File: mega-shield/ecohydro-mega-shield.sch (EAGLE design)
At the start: 99 parts, among them IC1 MCP1700-330, IC2 DS1306E, IC3 74HC125D, IC4 AP3211KTR, Q1 IRLM5103, Q10 PBSS4021NT,215, Q11 PBSS4021NT,215, Q12 PBSS4021NT,215, Q13 PBSS4021NT,215, Q14 PBSS4021NT,215, Q15 PBSS4021NT,215, Q16 PBSS4021NT,215, Q17 IRLM5103, Q18 IRLM5103, Q19 IRLM5103, Q2 IRLM5103, Q20 PBSS4021NT,215, Q21 PBSS4021NT,215, Q22 PBSS4021NT,215, Q3 IRLM5103, Q4 IRLM5103, Q5 IRLM5103, Q6 IRLM5103, Q7 IRLM5103, Q8 IRLM5103, Q9 PBSS4021NT,215, U1 ARDUINO-MEGA

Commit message: Rev 1.1 with some fixes, not sent for production yet
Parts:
- removed A7: MKDS1/3-3,81, con-phoenix-381:MKDS1/3-3,81
- added A15: MKDS1/3-3,81, con-phoenix-381:MKDS1/3-3,81
- BATT1: DIGIKEY (none) -> BK-883CT-ND
- C5: DIGIKEY (none) -> 490-1664-1-ND
- C6: DIGIKEY (none) -> 1276-2891-1-ND
- C7: DIGIKEY (none) -> 709-1231-1-ND
- D1: DIGIKEY (none) -> S1GFSCT-ND
- FS1, FS2: ATTRIBUTE 576-65800001109 -> (none); MOUSER (none) -> 576-65800001109
- IC1: DIGIKEY (none) -> AP1117IE33G-13DITR-ND
- IC2: DIGIKEY (none) -> DS1306EN+T&RCT-ND
- IC3: DIGIKEY (none) -> 568-1392-2-ND
- IC4: DIGIKEY (none) -> AP3211KTR-G1DICT-ND
- L1: DIGIKEY (none) -> 732-5536-1-ND
- Q10, Q11, Q12, Q13, Q14, Q15, Q16, Q20, Q21, Q22, Q9: DIGIKEY (none) -> PBSS4021NT,215
- R11, R12, R13, R14, R15, R16, R17, R18: DIGIKEY (none) -> 541-330ACT-ND
- R19: value 470R -> 1k; device passives:R-EU_R0603-N -> passives:R-EU_R0805
- R23: DIGIKEY (none) -> 541-49.9KCCT-ND
- R24: DIGIKEY (none) -> 541-9.53KCCT-ND
- Y1: DIGIKEY (none) -> 535-12051-1-ND
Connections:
- removed net N$5 (its old number): A7-2.1, U1.A7
- new net N$76: U1.3
- new net N$77: U1.2
- new net N$88: A15-2.1, U1.A15
- net GND: now also A15-3.1; no longer A7-3.1
- net N$10: now also A14-1.1; no longer A13-1.1
- net N$11: now also A13-1.1; no longer A12-1.1
- net N$12: now also A12-1.1; no longer A11-1.1
- net N$13: now also A11-1.1; no longer A10-1.1
- net N$14: now also U1.20(SDA); no longer U1.5
- net N$4: now also A8-1.1; no longer A7-1.1
- net N$6: now also A9-1.1; no longer A8-1.1
- net N$73: no longer U1.3
- net N$75: no longer U1.4
- net N$8: now also A10-1.1; no longer A9-1.1
- net N$9: now also A15-1.1; no longer A14-1.1
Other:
- moved on the sheet: A10-1, A10-2, A10-3, A11-1, A11-2, A11-3, A12-1, A12-2, A12-3, A13-1, A13-2, A13-3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

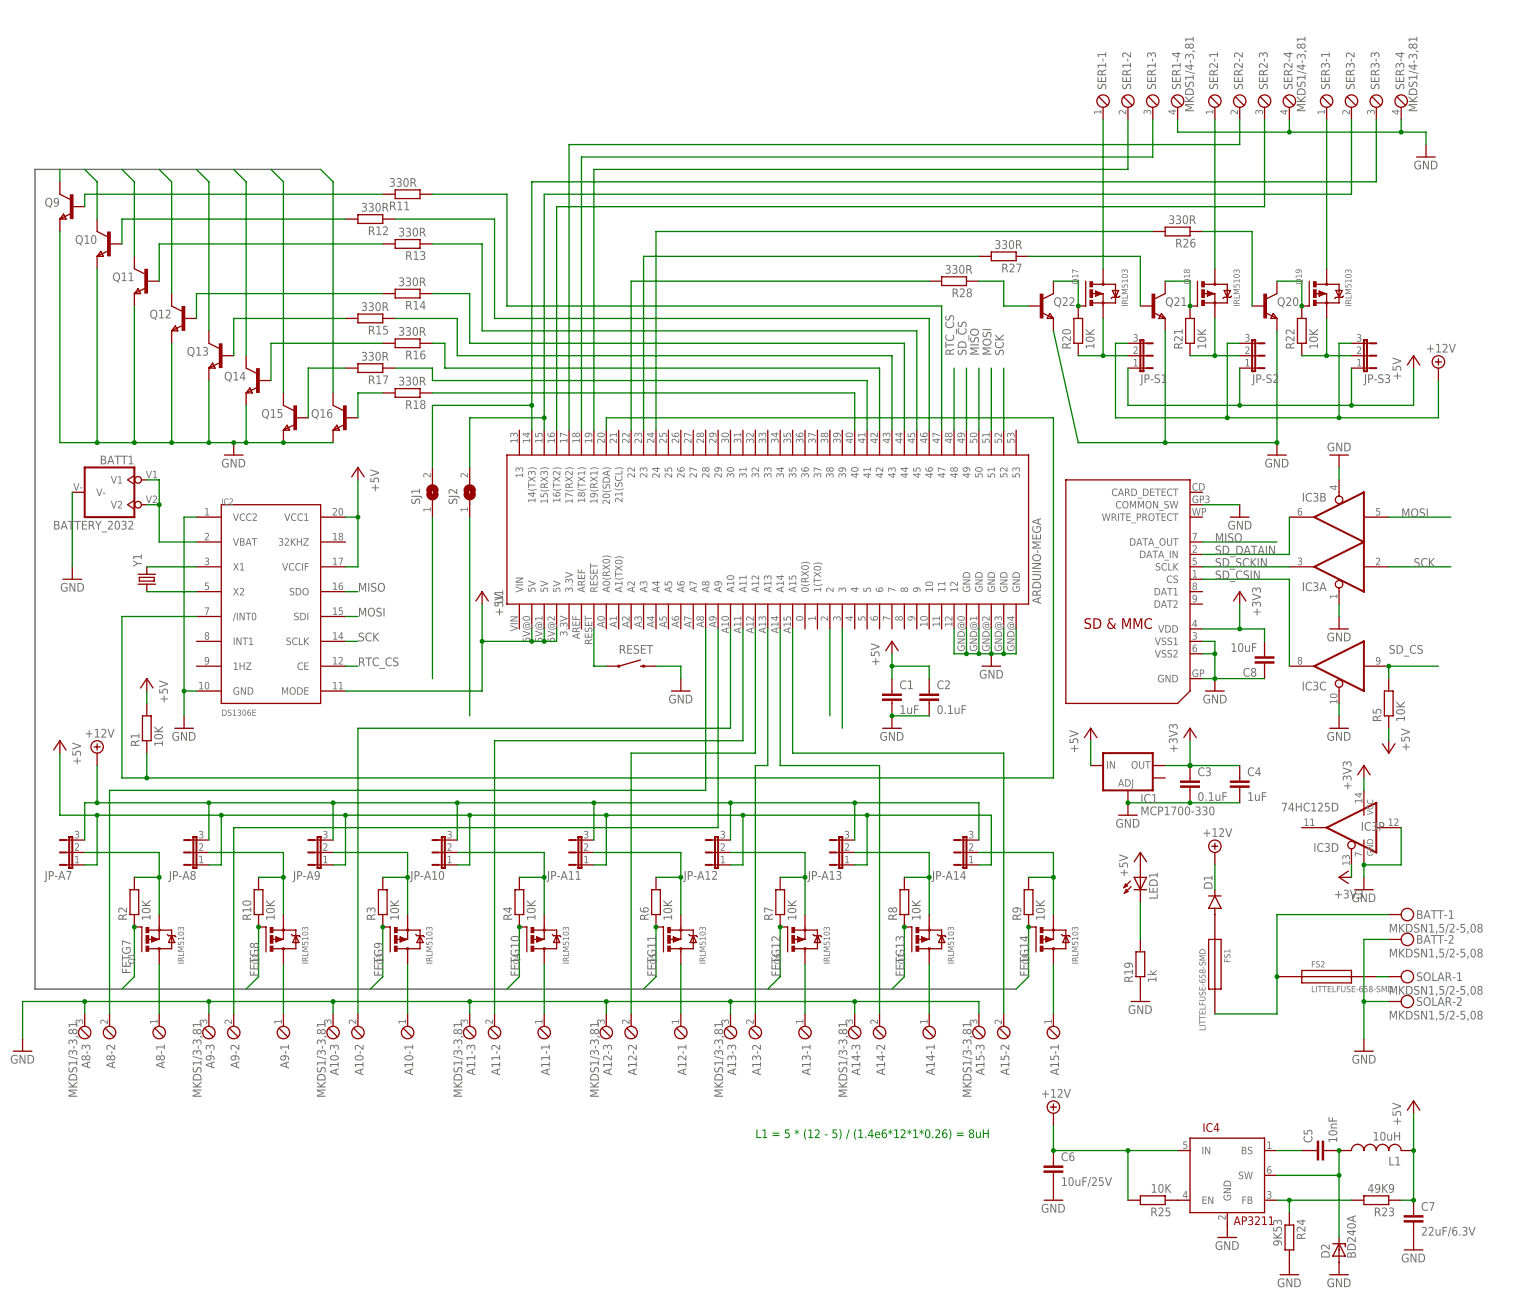
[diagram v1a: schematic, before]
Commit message: Rev 1.2 Fixes - Change R19 to 4k7 - GSM shield bypass pins are out by 1 (should be 2 & 3, not 3 & 4) - Change pads on Batt and Solar connectors - Change package on xtal
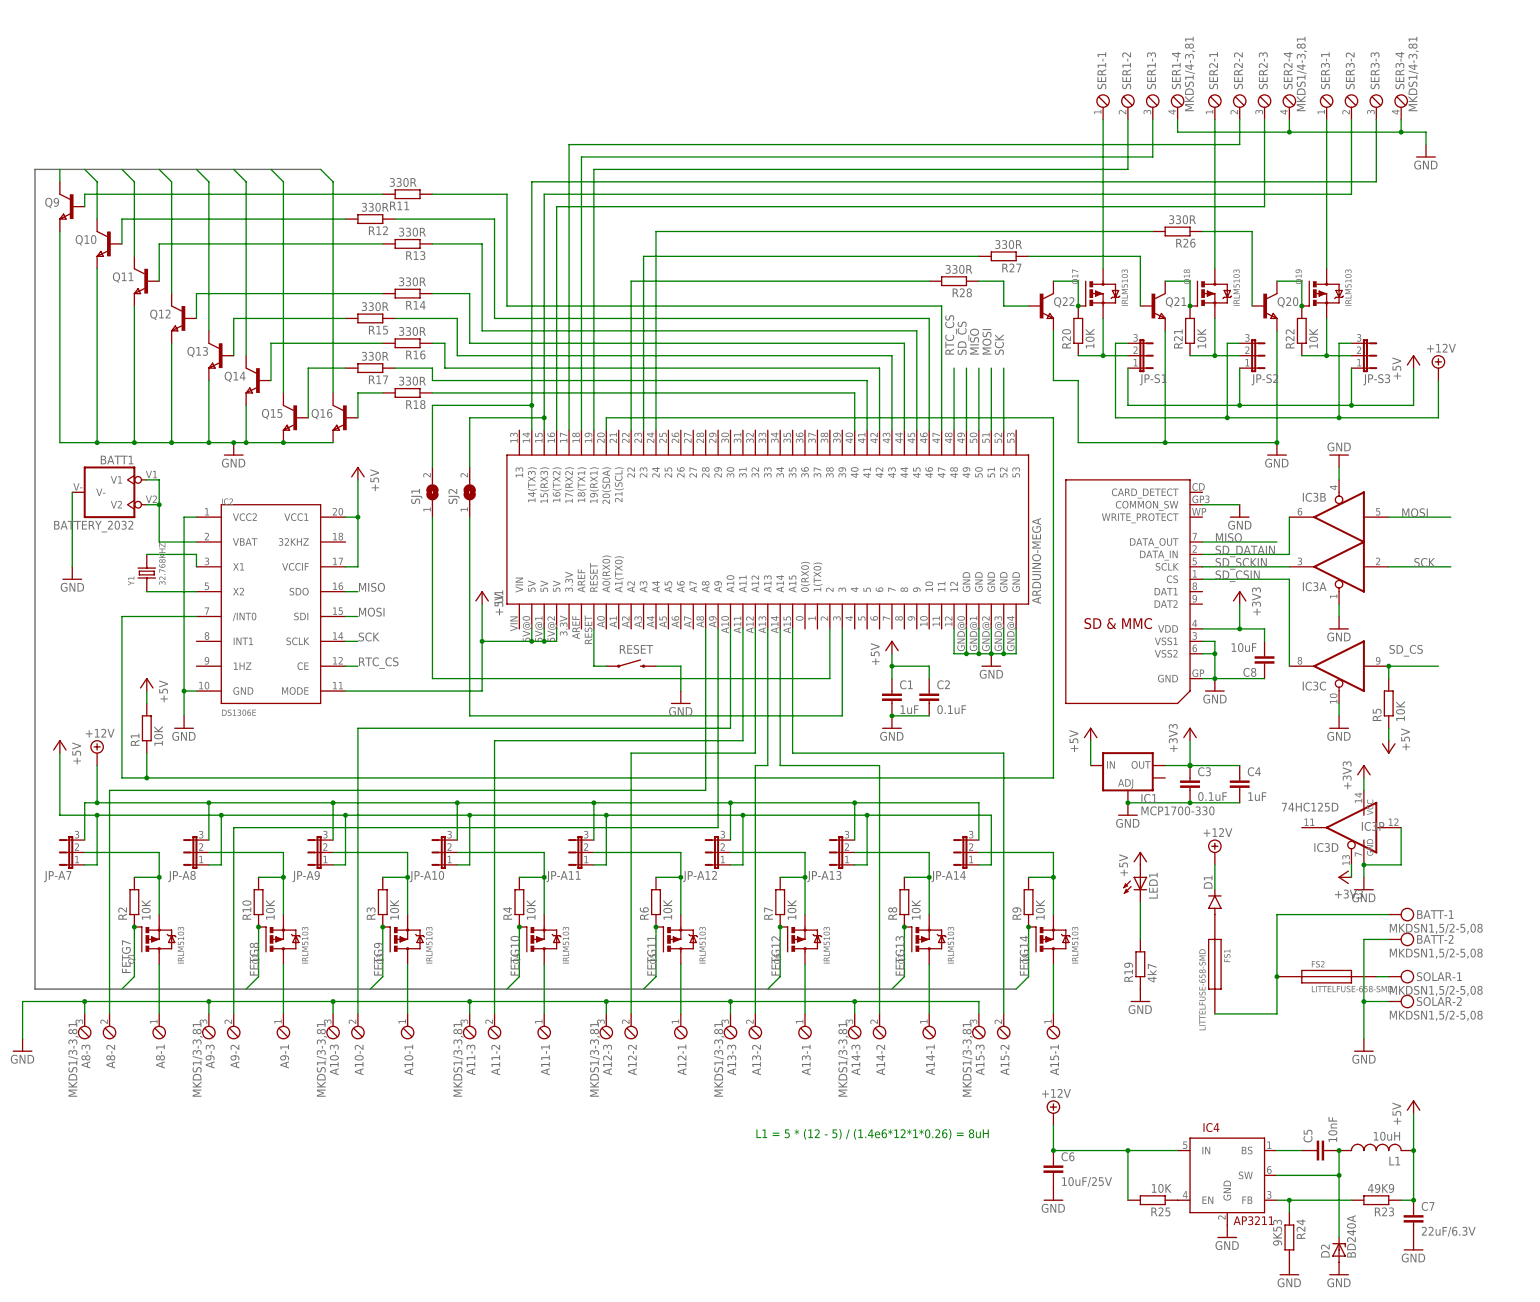
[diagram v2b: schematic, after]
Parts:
- BATT, SOLAR: device con-phoenix-508:MKDSN1,5/2-5,08 -> mechanical:MKDSN1,5/2-5,08
- R19: value 1k -> 4k7
- Y1: value (none) -> 32.768KHZ; device SparkFun-FreqCtrl:CRYSTAL32-SMD -> Seeed-Crystal Oscillator-2016:SMD-CRYSTAL-32.768KHZ-12.5PF-20PPM-90K(2P-L2.0X1.2MM)
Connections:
- removed net N$75: SJ1.1
- removed net N$76: U1.3
- net N$73: now also U1.3
- net N$77: now also SJ1.1
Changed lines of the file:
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@@
 <layer number="112" name="tSilk" color="7" fill="1" visible="yes" active="yes"/>
 <layer number="113" name="IDFDebug" color="4" fill="1" visible="yes" active="yes"/>
+<layer number="114" name="FRNTMAAT1" color="7" fill="1" visible="no" active="no"/>
+<layer number="115" name="FRNTMAAT2" color="7" fill="1" visible="no" active="no"/>
 <layer number="116" name="Patch_BOT" color="9" fill="4" visible="yes" active="yes"/>
+<layer number="117" name="BACKMAAT1" color="7" fill="1" visible="no" active="no"/>
 <layer number="118" name="Rect_Pads" color="7" fill="1" visible="no" active="no"/>
+<layer number="119" name="KAP_TEKEN" color="7" fill="1" visible="no" active="no"/>
+<layer number="120" name="KAP_MAAT1" color="7" fill="1" visible="no" active="no"/>
 <layer number="121" name="_tsilk" color="7" fill="1" visible="yes" active="yes"/>
 <layer number="122" name="_bsilk" color="7" fill="1" visible="yes" active="yes"/>
@@
 <layer number="127" name="_tValues" color="7" fill="1" visible="yes" active="yes"/>
 <layer number="128" name="_bValues" color="7" fill="1" visible="yes" active="yes"/>
+<layer number="129" name="top_silk" color="7" fill="1" visible="yes" active="yes"/>
+<layer number="130" name="SMDSTROOK" color="7" fill="1" visible="no" active="no"/>
 <layer number="131" name="tAdjust" color="7" fill="1" visible="no" active="yes"/>
 <layer number="132" name="bAdjust" color="7" fill="1" visible="no" active="yes"/>
+<layer number="133" name="bottom_silk" color="7" fill="1" visible="yes" active="yes"/>
 <layer number="144" name="Drill_legend" color="7" fill="1" visible="yes" active="yes"/>
 <layer number="150" name="Notes" color="7" fill="1" visible="no" active="yes"/>
@@
 <layer number="227" name="227bmp" color="7" fill="1" visible="no" active="yes"/>
 <layer number="228" name="228bmp" color="7" fill="1" visible="no" active="yes"/>
+<layer number="229" name="229bmp" color="7" fill="1" visible="yes" active="yes"/>
 <layer number="230" name="230bmp" color="7" fill="1" visible="no" active="yes"/>
+<layer number="231" name="Eagle3D_PG1" color="7" fill="1" visible="no" active="no"/>
+<layer number="232" name="Eagle3D_PG2" color="7" fill="1" visible="no" active="no"/>
+<layer number="233" name="Eagle3D_PG3" color="7" fill="1" visible="no" active="no"/>
 <layer number="248" name="Housing" color="7" fill="1" visible="yes" active="yes"/>
 <layer number="249" name="Edge" color="7" fill="1" visible="yes" active="yes"/>
@@
 <layer number="251" name="SMDround" color="7" fill="1" visible="no" active="no"/>
 <layer number="254" name="cooling" color="7" fill="1" visible="yes" active="yes"/>
+<layer number="255" name="Accent" color="7" fill="1" visible="no" active="no"/>
 </layers>
 <schematic>
@@
 <part name="P+3" library="supply1" deviceset="+5V" device=""/>
 <part name="GND1" library="supply1" deviceset="GND" device=""/>
-<part name="Y1" library="SparkFun-FreqCtrl" deviceset="CRYSTAL" device="32-SMD">
+<part name="Y1" library="Seeed-Crystal Oscillator-2016" deviceset="SMD-CRYSTAL-32.768KHZ-12.5PF-20PPM-90K(2P-L2.0X1.2MM)" device="" value="32.768KHZ">
 <attribute name="DIGIKEY" value="535-12051-1-ND"/>
 </part>
@@
 <attribute name="DIGIKEY" value="541-330ACT-ND "/>
 </part>
-<part name="BATT" library="con-phoenix-508" deviceset="MKDSN1,5/2-5,08" device=""/>
-<part name="SOLAR" library="con-phoenix-508" deviceset="MKDSN1,5/2-5,08" device=""/>
+<part name="BATT" library="mechanical" deviceset="MKDSN1,5/2-5,08" device=""/>
+<part name="SOLAR" library="mechanical" deviceset="MKDSN1,5/2-5,08" device=""/>
 <part name="GND9" library="supply1" deviceset="GND" device=""/>
 <part name="D1" library="SparkFun-DiscreteSemi" deviceset="DIODE" device="SMA">
@@
 <part name="GND10" library="supply1" deviceset="GND" device=""/>
 <part name="LED1" library="semiconductors" deviceset="LED" device="1206"/>
-<part name="R19" library="passives" deviceset="R-EU_" device="R0805" value="1k"/>
+<part name="R19" library="passives" deviceset="R-EU_" device="R0805" value="4k7"/>
 <part name="P+7" library="supply1" deviceset="+5V" device=""/>
 <part name="GND11" library="supply1" deviceset="GND" device=""/>
@@
 <instances>
 <instance part="P+1" gate="1" x="-10.16" y="83.82" rot="MR0"/>
-<instance part="GND2" gate="1" x="30.48" y="63.5"/>
+<instance part="GND2" gate="1" x="30.48" y="60.96"/>
 <instance part="C2" gate="G$1" x="81.28" y="63.5"/>
 <instance part="P+4" gate="1" x="73.66" y="73.66"/>
@@
 <instance part="P+3" gate="1" x="-35.56" y="109.22" rot="MR0"/>
 <instance part="GND1" gate="1" x="-71.12" y="55.88"/>
-<instance part="Y1" gate="G$1" x="-78.74" y="86.36" rot="R90">
-<attribute name="DIGIKEY" x="-78.74" y="86.36" size="1.778" layer="96" rot="R90" display="off"/>
+<instance part="Y1" gate="G$1" x="-78.74" y="87.63" rot="R90">
+<attribute name="DIGIKEY" x="-78.74" y="87.63" size="1.778" layer="96" rot="R90" display="off"/>
 </instance>
 <instance part="R1" gate="G$1" x="-78.74" y="55.88" rot="R90"/>
@@
 <segment>
 <pinref part="Q22" gate="G$1" pin="E"/>
-<wire x1="106.68" y1="137.16" x2="111.76" y2="114.3" width="0.1524" layer="91"/>
+<wire x1="106.68" y1="137.16" x2="106.68" y2="127" width="0.1524" layer="91"/>
+<wire x1="106.68" y1="127" x2="111.76" y2="127" width="0.1524" layer="91"/>
+<wire x1="111.76" y1="127" x2="111.76" y2="114.3" width="0.1524" layer="91"/>
 <wire x1="111.76" y1="114.3" x2="129.54" y2="114.3" width="0.1524" layer="91"/>
 <pinref part="Q20" gate="G$1" pin="E"/>
@@
 <segment>
 <pinref part="GND2" gate="1" pin="GND"/>
-<wire x1="30.48" y1="66.04" x2="30.48" y2="68.58" width="0.1524" layer="91"/>
+<wire x1="30.48" y1="63.5" x2="30.48" y2="68.58" width="0.1524" layer="91"/>
 <pinref part="RESET" gate="G$1" pin="2"/>
 <wire x1="30.48" y1="68.58" x2="25.4" y2="68.58" width="0.1524" layer="91"/>
@@
 <pinref part="U1" gate="G$1" pin="A15"/>
 <wire x1="53.34" y1="50.8" x2="53.34" y2="76.2" width="0.1524" layer="91"/>
-</segment>
-</net>
-<net name="N$1" class="0">
-<segment>
-<pinref part="Y1" gate="G$1" pin="2"/>
-<pinref part="IC2" gate="G$1" pin="X1"/>
-<wire x1="-78.74" y1="88.9" x2="-68.58" y2="88.9" width="0.1524" layer="91"/>
-</segment>
-</net>
-<net name="N$3" class="0">
-<segment>
-<pinref part="IC2" gate="G$1" pin="X2"/>
-<pinref part="Y1" gate="G$1" pin="1"/>
-<wire x1="-68.58" y1="83.82" x2="-78.74" y2="83.82" width="0.1524" layer="91"/>
 </segment>
 </net>
@@
 <pinref part="SJ2" gate="1" pin="1"/>
 <wire x1="-12.7" y1="99.06" x2="-12.7" y2="58.42" width="0.1524" layer="91"/>
-</segment>
-</net>
-<net name="N$75" class="0">
-<segment>
-<pinref part="SJ1" gate="1" pin="1"/>
-<wire x1="-20.32" y1="99.06" x2="-20.32" y2="66.04" width="0.1524" layer="91"/>
+<pinref part="U1" gate="G$1" pin="3"/>
+<wire x1="63.5" y1="76.2" x2="63.5" y2="58.42" width="0.1524" layer="91"/>
+<wire x1="-12.7" y1="58.42" x2="63.5" y2="58.42" width="0.1524" layer="91"/>
 </segment>
 </net>
@@
 </segment>
 </net>
-<net name="N$76" class="0">
-<segment>
-<pinref part="U1" gate="G$1" pin="3"/>
-<wire x1="63.5" y1="76.2" x2="63.5" y2="55.88" width="0.1524" layer="91"/>
-</segment>
-</net>
 <net name="N$77" class="0">
 <segment>
 <pinref part="U1" gate="G$1" pin="2"/>
-<wire x1="60.96" y1="58.42" x2="60.96" y2="76.2" width="0.1524" layer="91"/>
+<wire x1="60.96" y1="66.04" x2="60.96" y2="76.2" width="0.1524" layer="91"/>
+<pinref part="SJ1" gate="1" pin="1"/>
+<wire x1="-20.32" y1="99.06" x2="-20.32" y2="66.04" width="0.1524" layer="91"/>
+<wire x1="60.96" y1="66.04" x2="-20.32" y2="66.04" width="0.1524" layer="91"/>
 </segment>
 </net>
@@
 </segment>
 </net>
+<net name="N$1" class="0">
+<segment>
+<pinref part="Y1" gate="G$1" pin="1"/>
+<pinref part="IC2" gate="G$1" pin="X2"/>
+<wire x1="-78.74" y1="83.82" x2="-68.58" y2="83.82" width="0.1524" layer="91"/>
+</segment>
+</net>
+<net name="N$3" class="0">
+<segment>
+<pinref part="IC2" gate="G$1" pin="X1"/>
+<wire x1="-68.58" y1="88.9" x2="-68.58" y2="91.44" width="0.1524" layer="91"/>
+<pinref part="Y1" gate="G$1" pin="2"/>
+<wire x1="-68.58" y1="91.44" x2="-78.74" y2="91.44" width="0.1524" layer="91"/>
+</segment>
+</net>
